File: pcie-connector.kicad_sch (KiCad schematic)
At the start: 6 parts, among them J10 PCB-Edge_PCIexpress_x8, SW1 CVS-03B

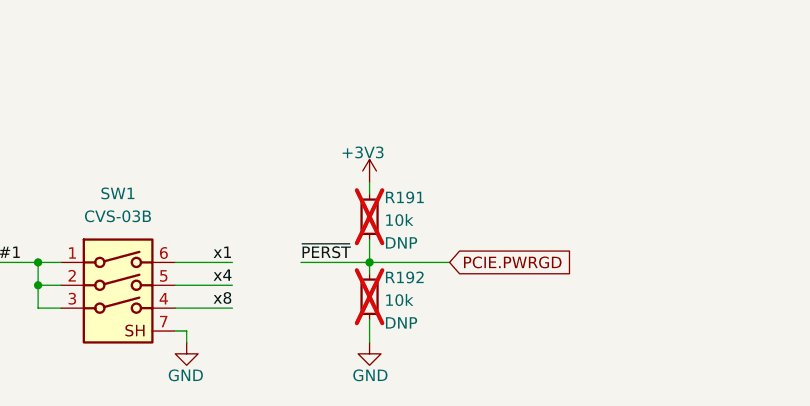
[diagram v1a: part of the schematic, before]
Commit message: [#69629] Fix DNP attributes
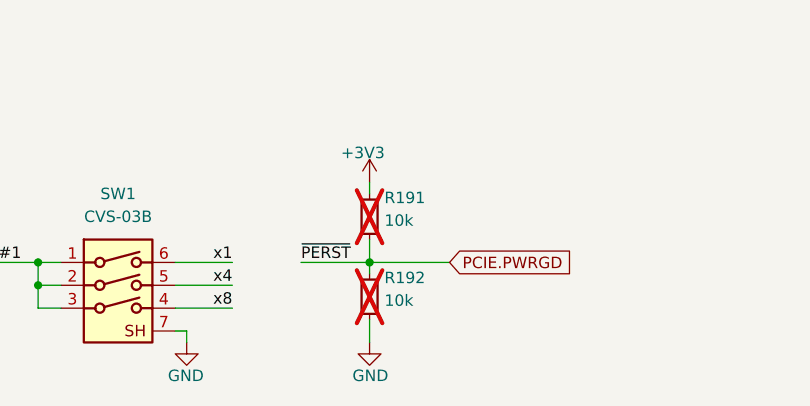
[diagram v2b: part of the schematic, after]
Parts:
- R191, R192: DNP DNP -> (none)
